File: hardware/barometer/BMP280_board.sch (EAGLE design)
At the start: 8 parts, among them U1 EM406FLAT

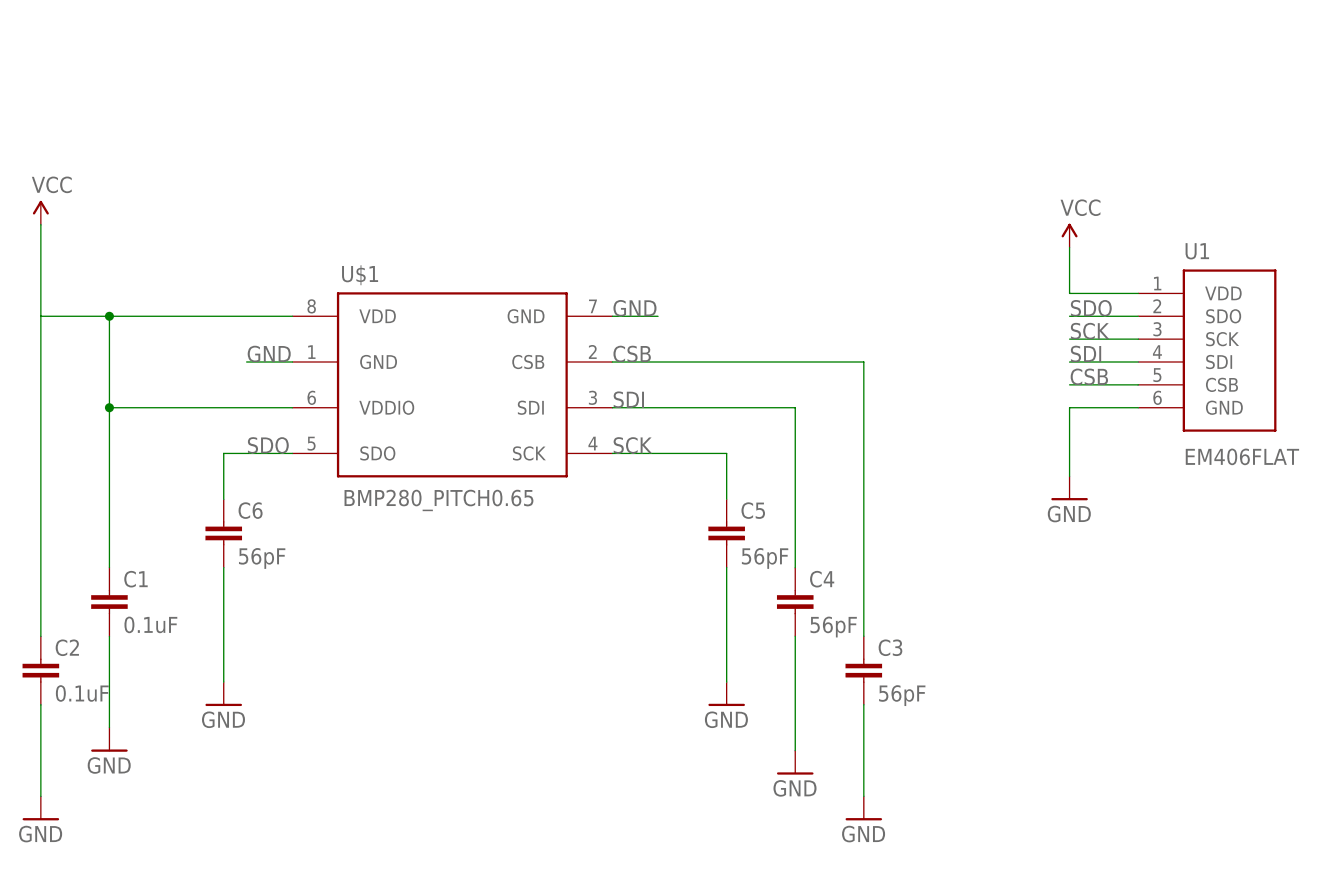
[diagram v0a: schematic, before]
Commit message: schematic layout
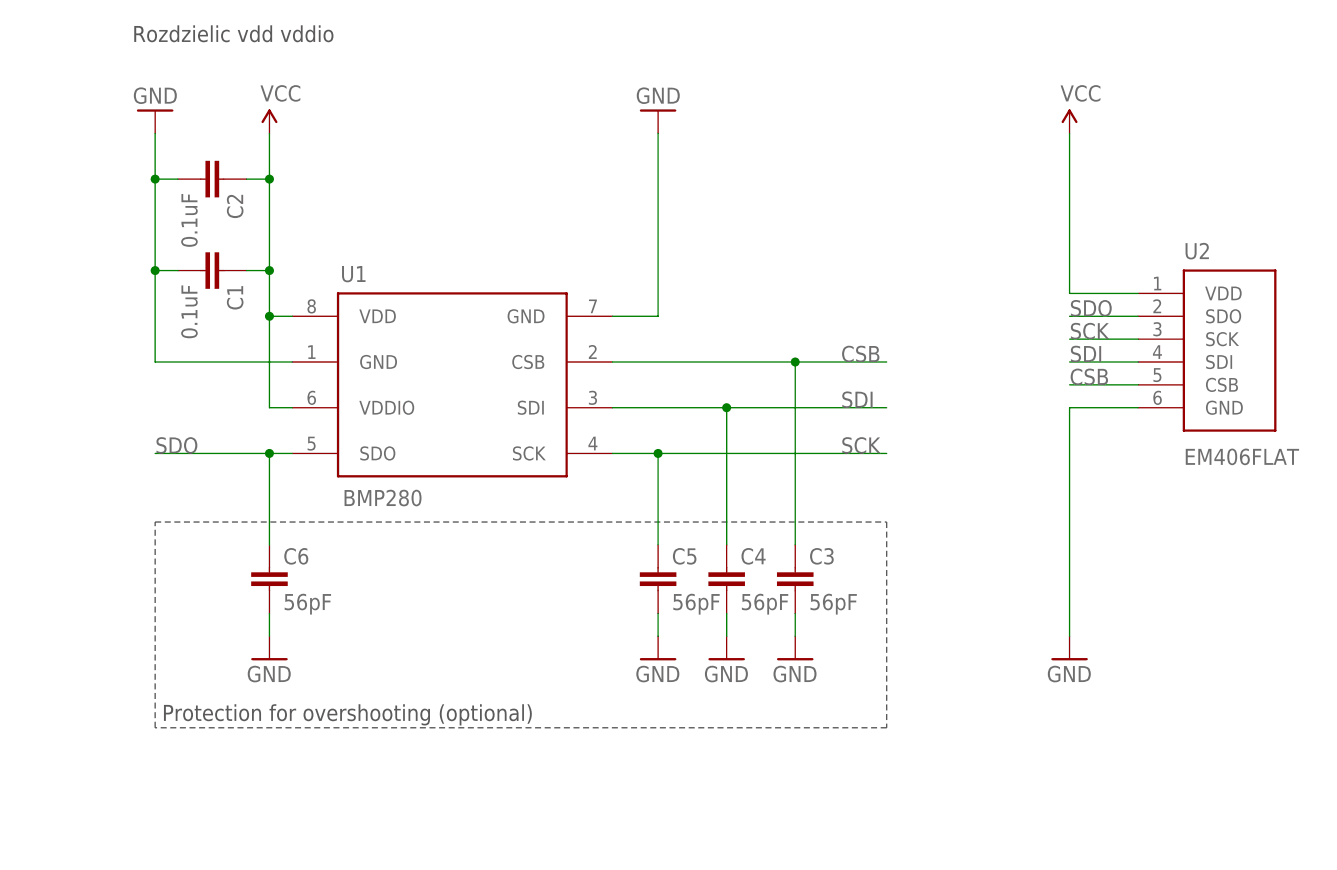
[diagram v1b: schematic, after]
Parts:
- removed U$1: BMP280_PITCH0.65, icarus_sensors:BMP280_PITCH0.65
- added U2: EM406FLAT, icarus_sensors:EM406FLAT
- U1: value EM406FLAT -> BMP280; device icarus_sensors:EM406FLAT -> icarus_sensors:BMP280_PITCH0.65
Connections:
- net CSB: now also U2.CSB; no longer U$1.CSB
- net GND: now also U1.GND@1, U1.GND@2, U2.GND; no longer U$1.GND@1, U$1.GND@2, U1.GND
- net SCK: now also U2.SCK; no longer U$1.SCK
- net SDI: now also U2.SDI; no longer U$1.SDI
- net SDO: now also U2.SDO; no longer U$1.SDO
- net VCC: now also U1.VDDIO, U2.VDD; no longer U$1.VDD, U$1.VDDIO
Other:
- note added: "Protection for overshooting (optional)"
- note added: "Rozdzielic vdd vddio"
- moved on the sheet: C1, C2, C3, C4, C5, C6
